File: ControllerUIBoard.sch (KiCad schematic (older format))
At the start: 27 parts, among them J10 UIBoardCON1, J11 SignalStrength, J9 ATMEGA_PROG, Q5 Q_PMOS_GSD, SW1 KeySwitch, U15 ATmega4809-A

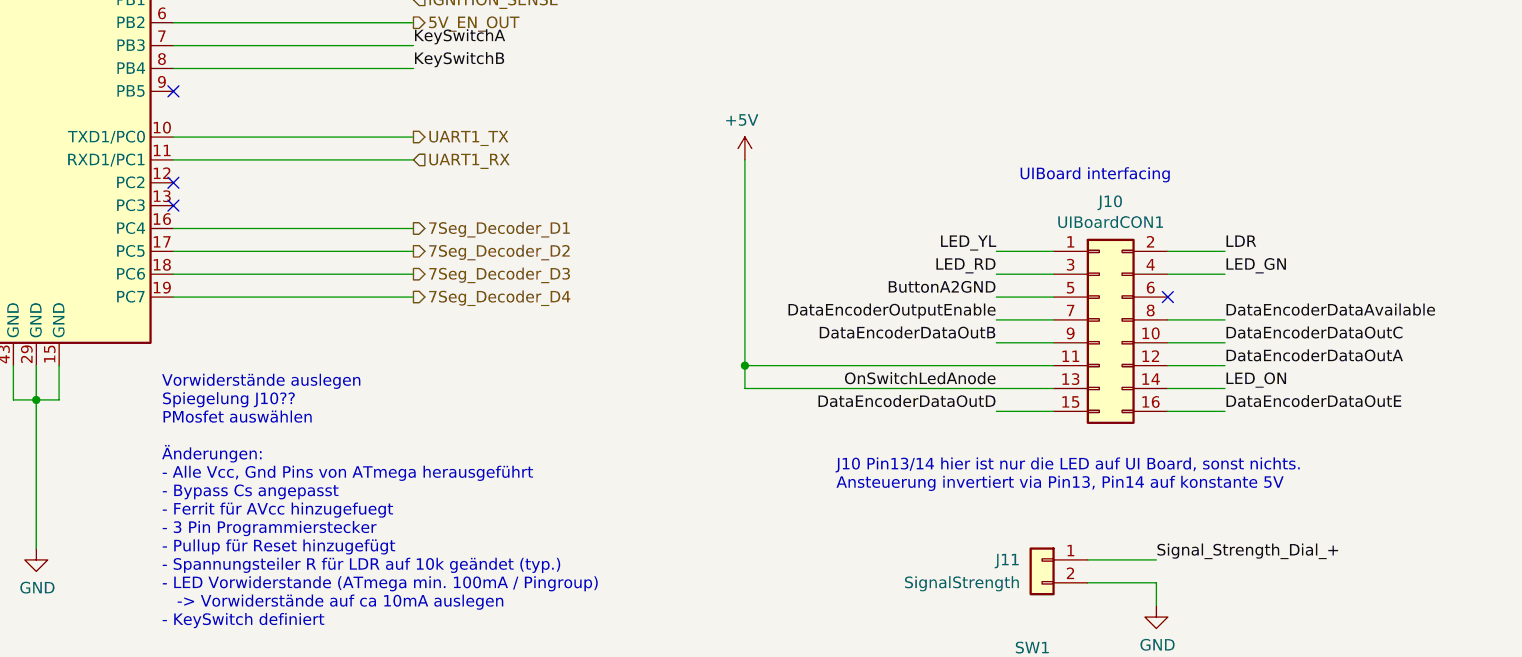
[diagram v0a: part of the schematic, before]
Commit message: - Signalnamen korrigiert, Spiegelung geprüft
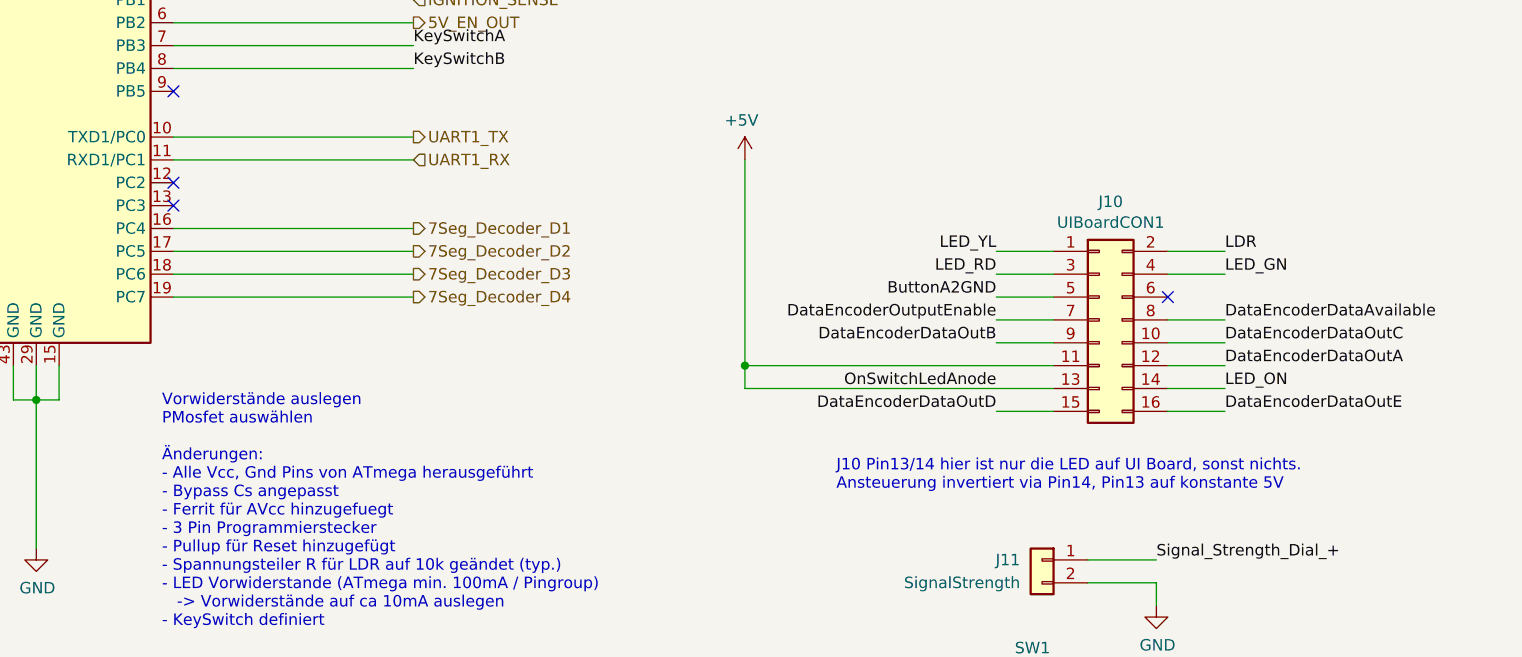
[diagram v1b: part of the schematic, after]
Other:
- note added: "J10 Pin13/14 hier ist nur die LED auf UI Board, sonst nichts.\nAnsteuerung invertiert via Pin14, Pin13 auf konstante 5V"
- note added: "Vorwiderstände auslegen\nPMosfet auswählen\n\nÄnderungen:\n- Alle Vcc, Gnd Pins von ATmega herausgeführt\n- Bypass Cs angepasst\n- Ferrit für AVcc hinzugefuegt\n- 3 Pin Programmierstecker\n- Pullup für Reset hinzugefügt\n- Spannungsteiler R für LDR auf 10k geändet (typ.)\n- LED Vorwiderstande (ATmega min. 100mA / Pingroup)\n -> Vorwiderstände auf ca 10mA auslegen\n- KeySwitch definiert"
- note removed: "J10 Pin13/14 hier ist nur die LED auf UI Board, sonst nichts.\nAnsteuerung invertiert via Pin13, Pin14 auf konstante 5V"
- note removed: "UIBoard interfacing\n"
- note removed: "Vorwiderstände auslegen\nSpiegelung J10??\nPMosfet auswählen\n\nÄnderungen:\n- Alle Vcc, Gnd Pins von ATmega herausgeführt\n- Bypass Cs angepasst\n- Ferrit für AVcc hinzugefuegt\n- 3 Pin Programmierstecker\n- Pullup für Reset hinzugefügt\n- Spannungsteiler R für LDR auf 10k geändet (typ.)\n- LED Vorwiderstande (ATmega min. 100mA / Pingroup)\n -> Vorwiderstände auf ca 10mA auslegen\n- KeySwitch de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"
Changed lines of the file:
@@
 Wire Wire Line
 	7800 4250 7800 3350
-Text Notes 9000 3450 0    50   ~ 0
-UIBoard interfacing\n
 Wire Wire Line
 	9600 5850 9300 5850
@@
 	4850 1100 4850 1450
 Text Notes 5250 5400 0    50   ~ 0
-Vorwiderstände auslegen\nSpiegelung J10??\nPMosfet auswählen\n\nÄnderungen:\n- Alle Vcc, Gnd Pins von ATmega herausgeführt\n- Bypass Cs angepasst\n- Ferrit für AVcc hinzugefuegt\n- 3 Pin Programmierstecker\n- Pullup für Reset hinzugefügt\n- Spannungsteiler R für LDR auf 10k geändet (typ.)\n- LED Vorwiderstande (ATmega min. 100mA / Pingroup)\n   -> Vorwiderstände auf ca 10mA auslegen\n- KeySwitch definiert
+Vorwiderstände auslegen\nPMosfet auswählen\n\nÄnderungen:\n- Alle Vcc, Gnd Pins von ATmega herausgeführt\n- Bypass Cs angepasst\n- Ferrit für AVcc hinzugefuegt\n- 3 Pin Programmierstecker\n- Pullup für Reset hinzugefügt\n- Spannungsteiler R für LDR auf 10k geändet (typ.)\n- LED Vorwiderstande (ATmega min. 100mA / Pingroup)\n   -> Vorwiderstände auf ca 10mA auslegen\n- KeySwitch definiert
 $Comp
 L Device:C C?
@@
 $EndComp
 Text Notes 8200 4800 0    50   ~ 0
-J10 Pin13/14 hier ist nur die LED auf UI Board, sonst nichts.\nAnsteuerung invertiert via Pin13, Pin14 auf konstante 5V
+J10 Pin13/14 hier ist nur die LED auf UI Board, sonst nichts.\nAnsteuerung invertiert via Pin14, Pin13 auf konstante 5V
 Wire Wire Line
 	7800 4350 7800 4250

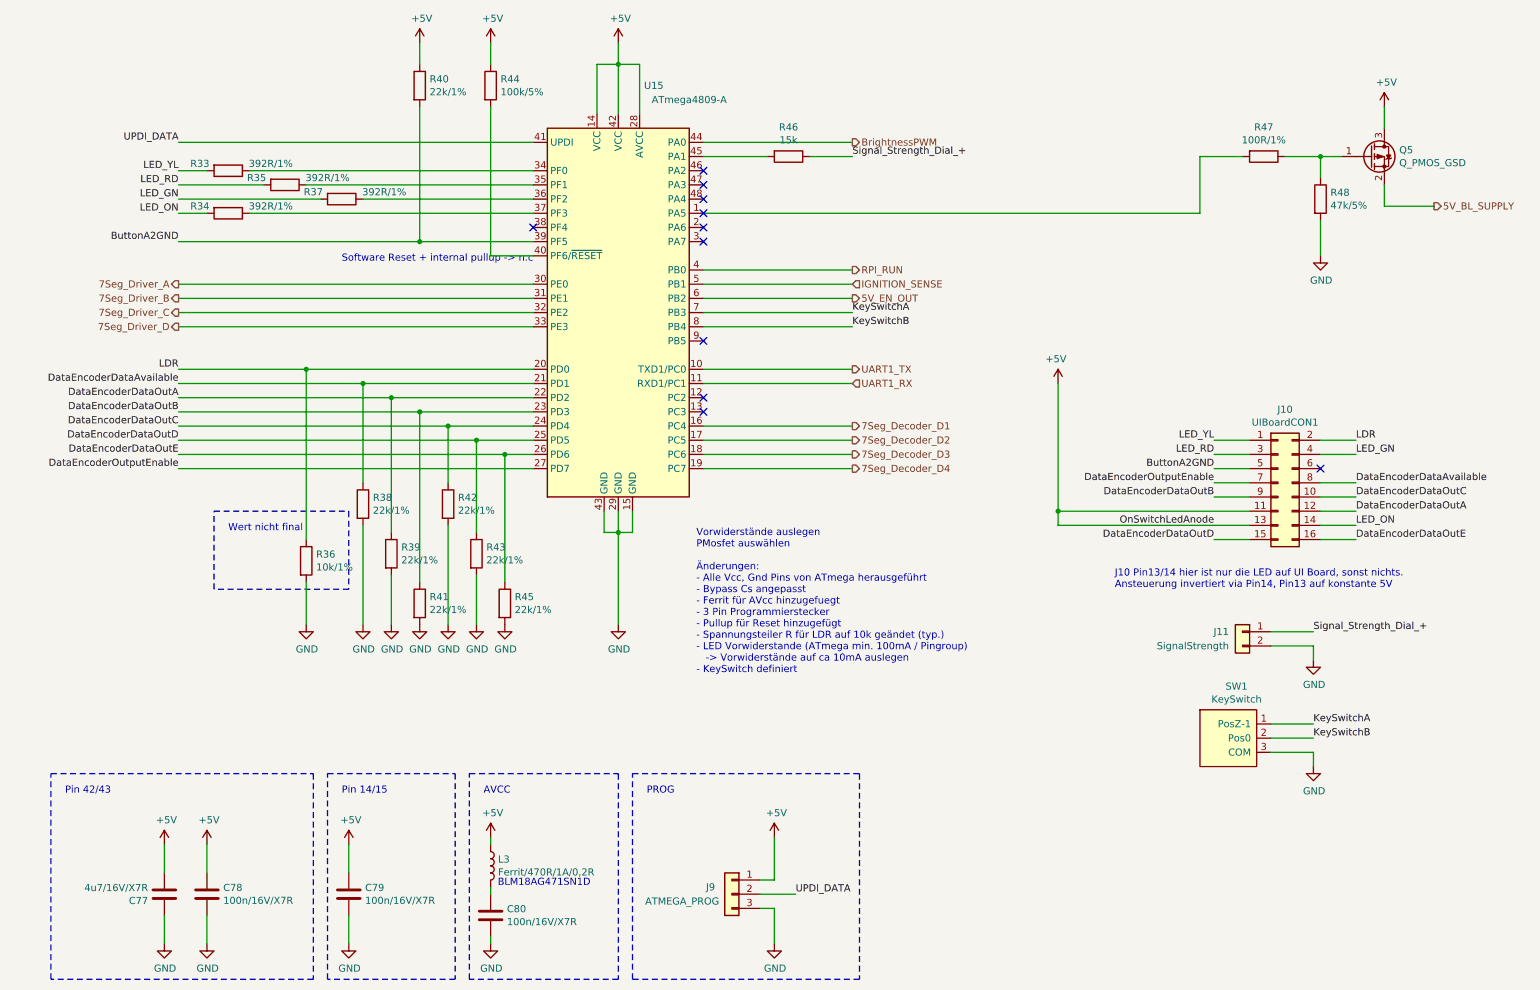
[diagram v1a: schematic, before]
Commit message: - Schaltbare BL Versorgung fertig - kleinere Value Anpassungen - Finale Annotation
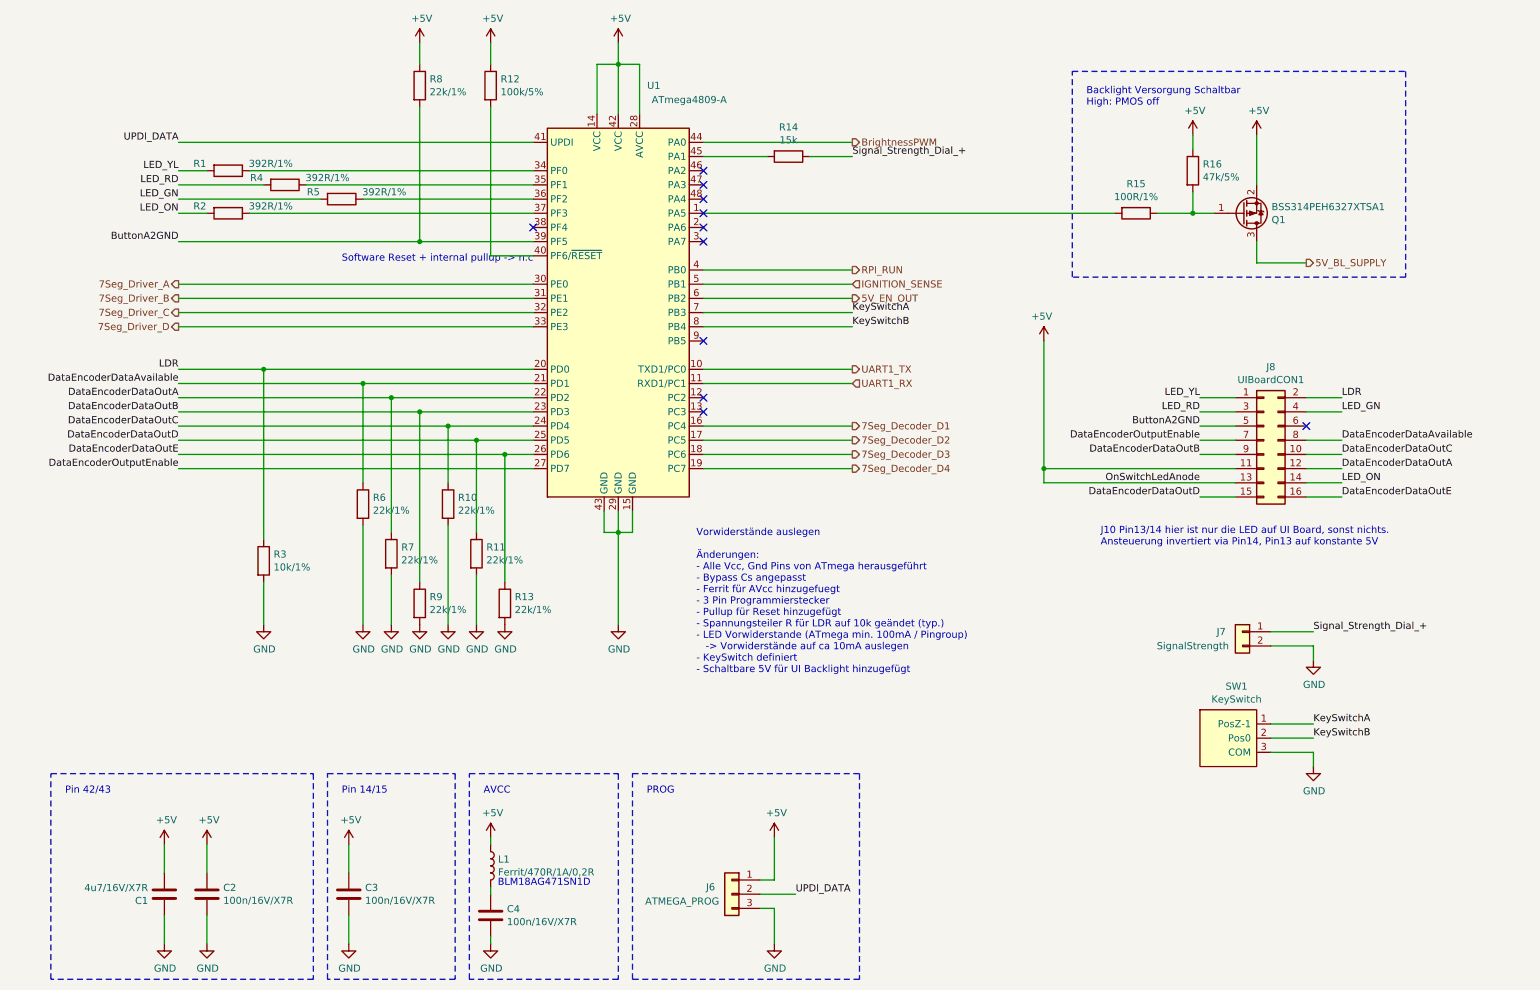
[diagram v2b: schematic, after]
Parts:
- Q1: renamed from Q5; value Q_PMOS_GSD -> BSS314PEH6327XTSA1; footprint (none) -> Package_TO_SOT_SMD:SOT-23
- renumbered C77 to C1, C78 to C2, C79 to C3, C80 to C4, J9 to J6, J11 to J7, J10 to J8, L3 to L1, R33 to R1, R42 to R10, R43 to R11, R44 to R12, R45 to R13, R46 to R14, R47 to R15, R48 to R16, R34 to R2, R36 to R3, R35 to R4, R37 to R5, R38 to R6, R39 to R7, R40 to R8, R41 to R9, U15 to U1
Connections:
- net +5V: now also Q1.2 (S), R16.1; no longer Q1.3 (D)
- net 5V_BL_SUPPLY: now also Q1.3 (D); no longer Q1.2 (S)
- net GND: no longer R16.2
- net at Q1.1 (G), R15.1: now also R16.2; no longer R16.1
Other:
- note added: "Backlight Versorgung Schaltbar\nHigh: PMOS off"
- note added: "Vorwiderstände auslegen\n\nÄnderungen:\n- Alle Vcc, Gnd Pins von ATmega herausgeführt\n- Bypass Cs angepasst\n- Ferrit für AVcc hinzugefuegt\n- 3 Pin Programmierstecker\n- Pullup für Reset hinzugefügt\n- Spannungsteiler R für LDR auf 10k geändet (typ.)\n- LED Vorwiderstande (ATmega min. 100mA / Pingroup)\n -> Vorwiderstände auf ca 10mA auslegen\n- KeySwitch definiert\n- Schaltbare 5V für UI Backl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"
- note removed: "Vorwiderstände auslegen\nPMosfet auswählen\n\nÄnderungen:\n- Alle Vcc, Gnd Pins von ATmega herausgeführt\n- Bypass Cs angepasst\n- Ferrit für AVcc hinzugefuegt\n- 3 Pin Programmierstecker\n- Pullup für Reset hinzugefügt\n- Spannungsteiler R für LDR auf 10k geändet (typ.)\n- LED Vorwiderstande (ATmega min. 100mA / Pingroup)\n -> Vorwiderstände auf ca 10mA auslegen\n- KeySwitch definiert"
- note removed: "Wert nicht final"
- moved on the sheet: J8, Q1, R15, R16, R3

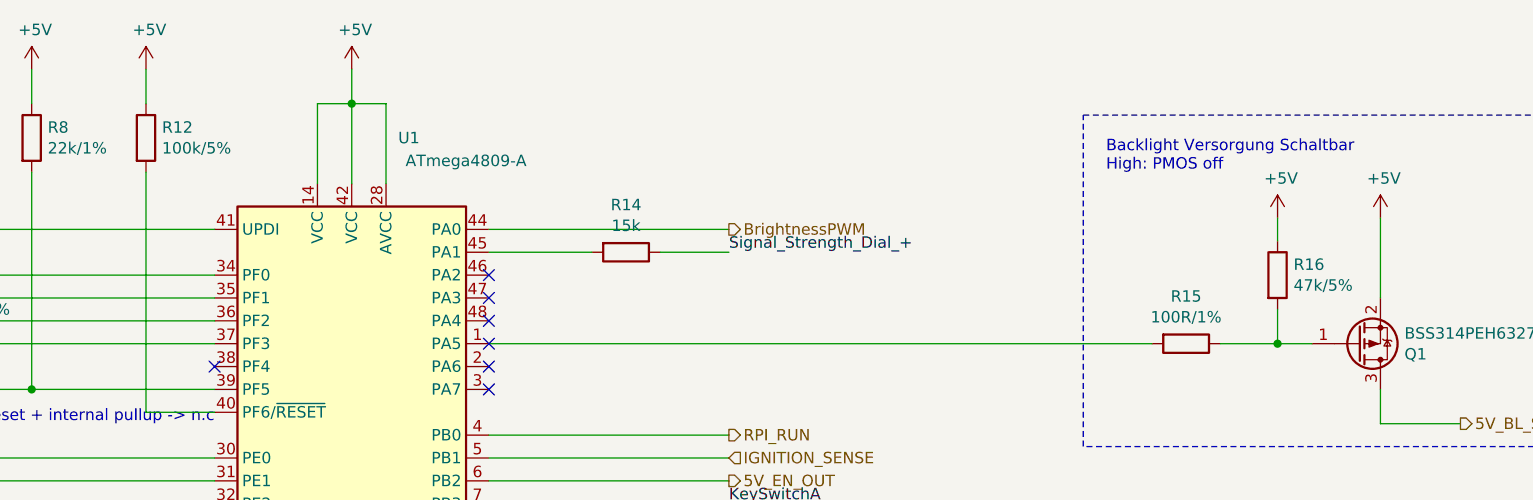
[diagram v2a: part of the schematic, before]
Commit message: - Bauteile konsolidiert
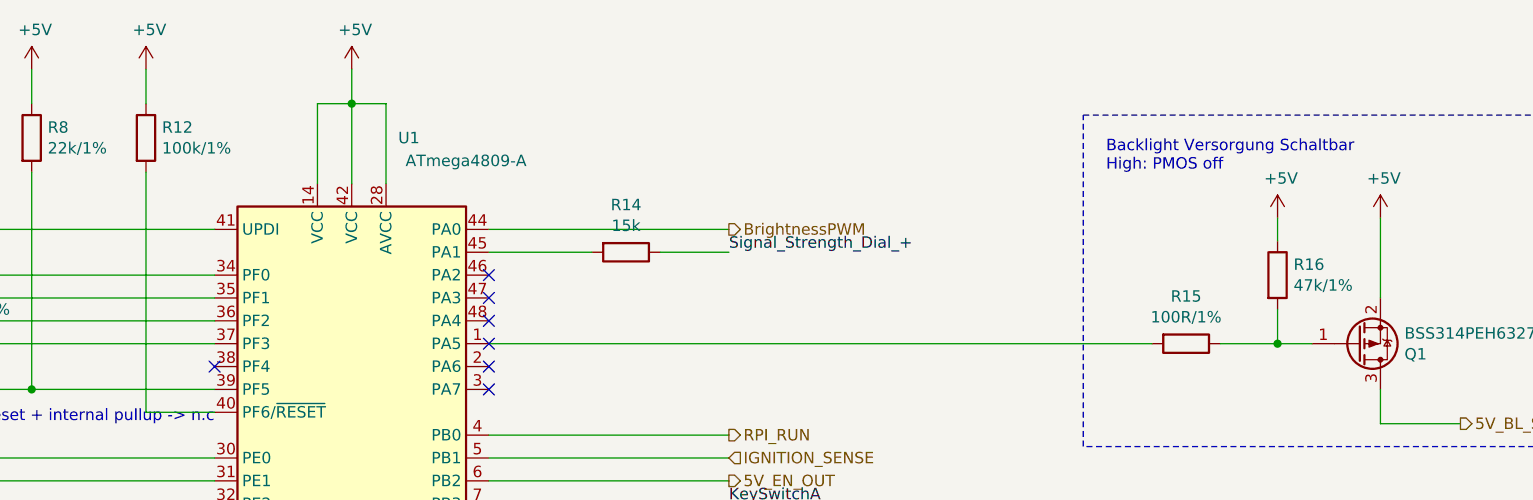
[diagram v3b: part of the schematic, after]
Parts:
- R12: value 100k/5% -> 100k/1%
- R16: value 47k/5% -> 47k/1%
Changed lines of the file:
@@
 P 3800 1250
 F 0 "R12" H 3870 1296 50  0000 L CNN
-F 1 "100k/5%" H 3870 1205 50  0000 L CNN
+F 1 "100k/1%" H 3870 1205 50  0000 L CNN
 F 2 "Resistor_SMD:R_0402_1005Metric" V 3730 1250 50  0001 C CNN
 F 3 "~" H 3800 1250 50  0001 C CNN
@@
 P 8750 1850
 F 0 "R16" H 8820 1896 50  0000 L CNN
-F 1 "47k/5%" H 8820 1805 50  0000 L CNN
+F 1 "47k/1%" H 8820 1805 50  0000 L CNN
 F 2 "Resistor_SMD:R_0402_1005Metric" V 8680 1850 50  0001 C CNN
 F 3 "~" H 8750 1850 50  0001 C CNN
